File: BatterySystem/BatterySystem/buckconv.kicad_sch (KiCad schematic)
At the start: 0 parts

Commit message: DCDC Converter symbol & footprint
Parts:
- added U1: 3.3V, VR20S3V3:VR20S3V3, symbol custom:VR20S3V3
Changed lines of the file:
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@@
 (kicad_sch (version 20230121) (generator eeschema)
   (paper "A4")
+  (symbol (lib_id "custom:VR20S3V3") (at 135.89 80.01 0) (unit 1)
+    (in_bom yes) (on_board yes) (dnp no) (fields_autoplaced)
+    (property "Reference" "U1" (at 141.605 80.3268 0)
+      (effects (font (size 1.27 1.27)) (justify left))
+    )
+    (property "Value" "3.3V" (at 135.89 80.01 0)
+      (effects (font (size 1.27 1.27)) hide)
+    )
+    (property "Footprint" "VR20S3V3:VR20S3V3" (at 135.89 80.01 0)
+      (effects (font (size 1.27 1.27)) hide)
+    )
+    (property "Datasheet" "https://www.farnell.com/datasheets/3103815.pdf" (at 135.89 80.01 0)
+      (effects (font (size 1.27 1.27)) hide)
+    )
+    (pin "2")
+    (pin "3")
+    (pin "1")
+    (instances
+      (project "BatterySystem"
+        (path "/087df5f5-f8bd-4aad-837d-9ee553cf1b81/a03965c6-cfc0-427e-8817-8deee22f0563"
+          (reference "U1") (unit 1)
+        )
+      )
+    )
+  )
 )

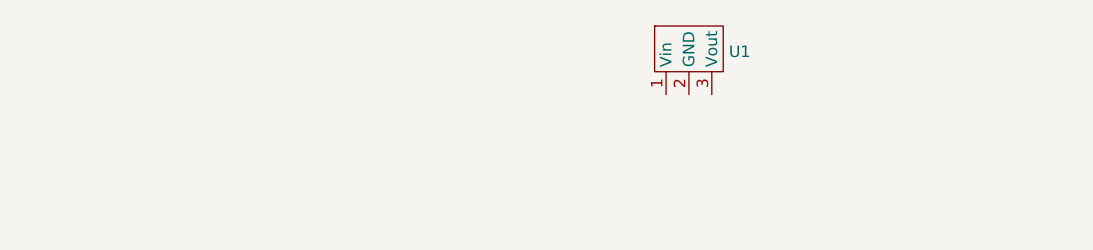
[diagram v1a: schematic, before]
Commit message: Circuit  of the DCDC conv
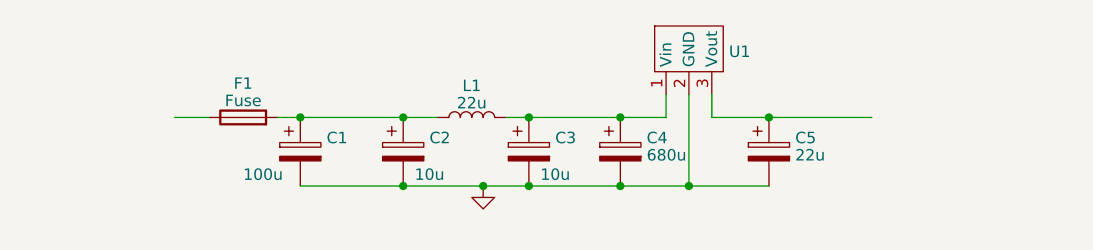
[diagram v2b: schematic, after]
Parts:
- added C1: 100u, symbol Device:C_Polarized
- added C2, C3: 10u, symbol Device:C_Polarized
- added C4: 680u, symbol Device:C_Polarized
- added C5: 22u, symbol Device:C_Polarized
- added F1: Fuse, symbol Device:Fuse
- added L1: 22u, symbol Device:L
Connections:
- net at U1.1 (Vin): now also C3.1, C4.1, L1.2
- net GND: now reaches U1.2 (GND)
- net GND: now also C1.2, C2.2, C3.2, C4.2, C5.2
- net at U1.3 (Vout): now also C5.1
- new net: C1.1, C2.1, F1.2, L1.1

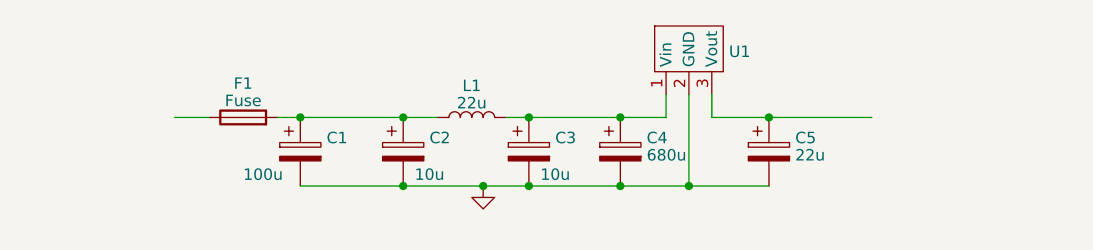
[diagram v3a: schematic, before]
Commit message: USB toegevoegd
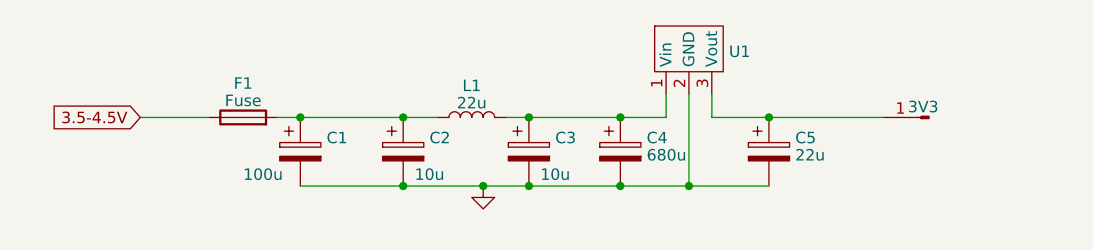
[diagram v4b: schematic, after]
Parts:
- added 3V3: Conn_01x01_Pin, symbol Connector:Conn_01x01_Pin
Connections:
- net at C5.1, U1.3 (Vout): now also 3V3.1 (Pin_1)
- net 3.5-4.5V: now reaches F1.1
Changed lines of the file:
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@@
-    (stroke (width 0) (type default))
-  )
-  (wire (pts (xy 146.05 87.63) (xy 157.48 87.63))
     (stroke (width 0) (type default))
   )
@@
     (stroke (width 0) (type default))
   )
-  (wire (pts (xy 80.01 87.63) (xy 83.82 87.63))
+  (wire (pts (xy 146.05 87.63) (xy 158.75 87.63))
     (stroke (width 0) (type default))
   )
   (wire (pts (xy 137.16 85.09) (xy 137.16 95.25))
+    (stroke (width 0) (type default))
+  )
+  (wire (pts (xy 76.2 87.63) (xy 83.82 87.63))
     (stroke (width 0) (type default))
   )
@@
   (wire (pts (xy 93.98 87.63) (xy 105.41 87.63))
     (stroke (width 0) (type default))
+  )
+  (global_label "3.5-4.5V" (shape input) (at 76.2 87.63 180) (fields_autoplaced)
+    (effects (font (size 1.27 1.27)) (justify right))
+    (property "Intersheetrefs" "${INTERSHEET_REFS}" (at 64.5856 87.63 0)
+      (effects (font (size 1.27 1.27)) (justify right) hide)
+    )
   )
   (symbol (lib_id "Device:C_Polarized") (at 93.98 91.44 0) (unit 1)
@@
         )
       )
+    )
+  )
+  (symbol (lib_id "Connector:Conn_01x01_Pin") (at 163.83 87.63 180) (unit 1)
+    (in_bom yes) (on_board yes) (dnp no) (fields_autoplaced)
+    (property "Reference" "3V3" (at 163.195 86.4649 0)
+      (effects (font (size 1.27 1.27)))
+    )
+    (property "Value" "Conn_01x01_Pin" (at 163.195 88.7951 0)
+      (effects (font (size 1.27 1.27)) hide)
+    )
+    (property "Footprint" "" (at 163.83 87.63 0)
+      (effects (font (size 1.27 1.27)) hide)
+    )
+    (property "Datasheet" "~" (at 163.83 87.63 0)
+      (effects (font (size 1.27 1.27)) hide)
+    )
+    (pin "1")
+    (instances
+      (project "BatterySystem"
+        (path "/087df5f5-f8bd-4aad-837d-9ee553cf1b81/a03965c6-cfc0-427e-8817-8deee22f0563"
+          (reference "3V3") (unit 1)
+        )
+      )

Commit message: footprint buckconv
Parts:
- C1: footprint (none) -> Capacitor_THT:CP_Radial_D8.0mm_P3.50mm
- C2, C3: footprint (none) -> Capacitor_SMD:C_1206_3216Metric
- C4: footprint (none) -> Capacitor_THT:CP_Radial_D12.5mm_P5.00mm
- C5: footprint (none) -> Capacitor_SMD:C_0805_2012Metric
- L1: footprint (none) -> Inductor_SMD:L_Bourns_SRP1038C_10.0x10.0mm
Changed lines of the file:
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@@
       (effects (font (size 1.27 1.27)) (justify left))
     )
-    (property "Footprint" "" (at 94.9452 95.25 0)
+    (property "Footprint" "Capacitor_THT:CP_Radial_D8.0mm_P3.50mm" (at 94.9452 95.25 0)
       (effects (font (size 1.27 1.27)) hide)
     )
@@
       (effects (font (size 1.27 1.27)) (justify left))
     )
-    (property "Footprint" "" (at 120.3452 95.25 0)
+    (property "Footprint" "Capacitor_SMD:C_1206_3216Metric" (at 120.3452 95.25 0)
       (effects (font (size 1.27 1.27)) hide)
     )
@@
       (effects (font (size 1.27 1.27)) (justify left))
     )
-    (property "Footprint" "" (at 147.0152 95.25 0)
+    (property "Footprint" "Capacitor_SMD:C_0805_2012Metric" (at 147.0152 95.25 0)
       (effects (font (size 1.27 1.27)) hide)
     )
@@
       (effects (font (size 1.27 1.27)) (justify left))
     )
-    (property "Footprint" "" (at 106.3752 95.25 0)
+    (property "Footprint" "Capacitor_SMD:C_1206_3216Metric" (at 106.3752 95.25 0)
       (effects (font (size 1.27 1.27)) hide)
     )
@@
       (effects (font (size 1.27 1.27)))
     )
-    (property "Footprint" "" (at 113.03 87.63 0)
+    (property "Footprint" "Inductor_SMD:L_Bourns_SRP1038C_10.0x10.0mm" (at 113.03 87.63 0)
       (effects (font (size 1.27 1.27)) hide)
     )
@@
       (effects (font (size 1.27 1.27)) (justify left))
     )
-    (property "Footprint" "" (at 130.5052 95.25 0)
+    (property "Footprint" "Capacitor_THT:CP_Radial_D12.5mm_P5.00mm" (at 130.5052 95.25 0)
       (effects (font (size 1.27 1.27)) hide)
     )

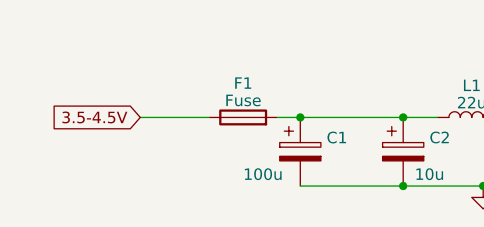
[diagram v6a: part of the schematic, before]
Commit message: Batterij en houder toegevoegd
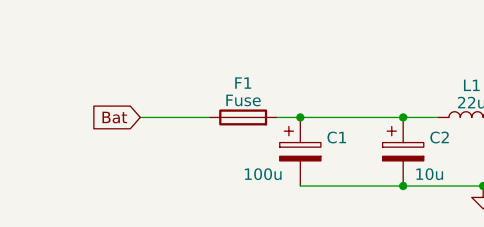
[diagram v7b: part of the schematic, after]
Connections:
- net 3.5-4.5V renamed Bat
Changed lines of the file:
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@@
     (stroke (width 0) (type default))
   )
-  (global_label "3.5-4.5V" (shape input) (at 76.2 87.63 180) (fields_autoplaced)
+  (global_label "Bat" (shape input) (at 76.2 87.63 180) (fields_autoplaced)
     (effects (font (size 1.27 1.27)) (justify right))
-    (property "Intersheetrefs" "${INTERSHEET_REFS}" (at 64.5856 87.63 0)
+    (property "Intersheetrefs" "${INTERSHEET_REFS}" (at 70.1495 87.63 0)
       (effects (font (size 1.27 1.27)) (justify right) hide)
     )

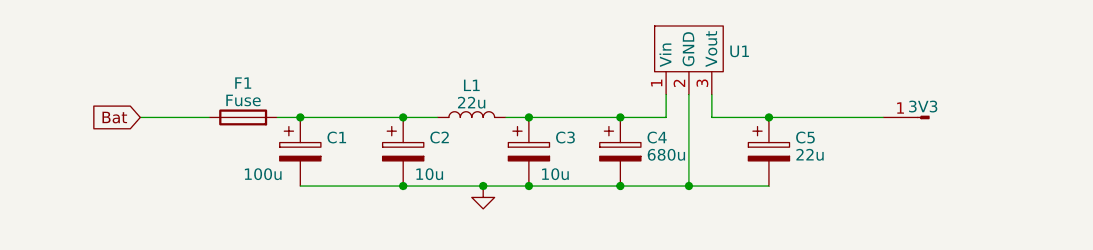
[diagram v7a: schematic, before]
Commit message: Componenten footprint toegevoegd
usb c footprint is met niks aangesloten. raar
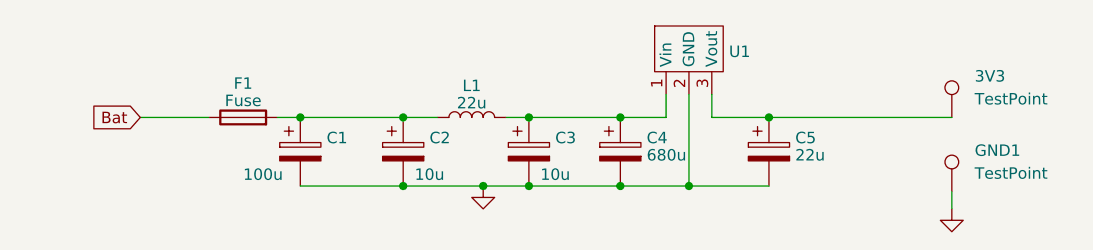
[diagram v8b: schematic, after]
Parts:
- removed 3V3: Conn_01x01_Pin, symbol Connector:Conn_01x01_Pin
- added 3V3, GND1: TestPoint, TestPoint:TestPoint_Keystone_5005-5009_Compact, symbol Connector:TestPoint
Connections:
- net GND: now also GND1.1
- net at C5.1, U1.3 (Vout): now also 3V3.1
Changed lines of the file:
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@@
+    (stroke (width 0) (type default))
+  )
+  (wire (pts (xy 166.37 95.885) (xy 166.37 97.79))
     (stroke (width 0) (type default))
   )
@@
     (stroke (width 0) (type default))
   )
-  (wire (pts (xy 146.05 87.63) (xy 158.75 87.63))
+  (wire (pts (xy 146.05 87.63) (xy 166.37 87.63))
     (stroke (width 0) (type default))
   )
@@
     )
   )
-  (symbol (lib_id "Connector:Conn_01x01_Pin") (at 163.83 87.63 180) (unit 1)
-    (in_bom yes) (on_board yes) (dnp no) (fields_autoplaced)
-    (property "Reference" "3V3" (at 163.195 86.4649 0)
-      (effects (font (size 1.27 1.27)))
-    )
-    (property "Value" "Conn_01x01_Pin" (at 163.195 88.7951 0)
-      (effects (font (size 1.27 1.27)) hide)
-    )
-    (property "Footprint" "" (at 163.83 87.63 0)
-      (effects (font (size 1.27 1.27)) hide)
-    )
-    (property "Datasheet" "~" (at 163.83 87.63 0)
-      (effects (font (size 1.27 1.27)) hide)
-    )
-    (pin "1")
-    (instances
-      (project "BatterySystem"
-        (path "/087df5f5-f8bd-4aad-837d-9ee553cf1b81/a03965c6-cfc0-427e-8817-8deee22f0563"
-          (reference "3V3") (unit 1)
-        )
-      )
-    )
-  )
   (symbol (lib_id "Device:C_Polarized") (at 105.41 91.44 0) (unit 1)
     (in_bom yes) (on_board yes) (dnp no)
@@
     )
   )
+  (symbol (lib_id "Connector:TestPoint") (at 166.37 95.885 0) (unit 1)
+    (in_bom yes) (on_board yes) (dnp no) (fields_autoplaced)
+    (property "Reference" "GND1" (at 168.91 91.313 0)
+      (effects (font (size 1.27 1.27)) (justify left))
+    )
+    (property "Value" "TestPoint" (at 168.91 93.853 0)
+      (effects (font (size 1.27 1.27)) (justify left))
+    )
+    (property "Footprint" "TestPoint:TestPoint_Keystone_5005-5009_Compact" (at 171.45 95.885 0)
+      (effects (font (size 1.27 1.27)) hide)
+    )
+    (property "Datasheet" "~" (at 171.45 95.885 0)
+      (effects (font (size 1.27 1.27)) hide)
+    )
+    (pin "1")
+    (instances
+      (project "BatterySystem"
+        (path "/087df5f5-f8bd-4aad-837d-9ee553cf1b81/a03965c6-cfc0-427e-8817-8deee22f0563"
+          (reference "GND1") (unit 1)
+        )
+      )
+    )
+  )
+  (symbol (lib_id "power:GND") (at 166.37 97.79 0) (unit 1)
+    (in_bom yes) (on_board yes) (dnp no) (fields_autoplaced)
+    (property "Reference" "#PWR013" (at 166.37 104.14 0)
+      (effects (font (size 1.27 1.27)) hide)
+    )
+    (property "Value" "GND" (at 166.37 101.9255 0)
+      (effects (font (size 1.27 1.27)) hide)
+    )
+    (property "Footprint" "" (at 166.37 97.79 0)
+      (effects (font (size 1.27 1.27)) hide)
+    )
+    (property "Datasheet" "" (at 166.37 97.79 0)
+      (effects (font (size 1.27 1.27)) hide)
+    )
+    (pin "1")
+    (instances
+      (project "BatterySystem"
+        (path "/087df5f5-f8bd-4aad-837d-9ee553cf1b81/a03965c6-cfc0-427e-8817-8deee22f0563"
+          (reference "#PWR013") (unit 1)
+        )
+      )
+    )
+  )
   (symbol (lib_id "Device:L") (at 113.03 87.63 90) (unit 1)
     (in_bom yes) (on_board yes) (dnp no) (fields_autoplaced)
@@
         )
       )
+    )
+  )
+  (symbol (lib_id "Connector:TestPoint") (at 166.37 87.63 0) (unit 1)
+    (in_bom yes) (on_board yes) (dnp no) (fields_autoplaced)
+    (property "Reference" "3V3" (at 168.91 83.058 0)
+      (effects (font (size 1.27 1.27)) (justify left))
+    )
+    (property "Value" "TestPoint" (at 168.91 85.598 0)
+      (effects (font (size 1.27 1.27)) (justify left))
+    )
+    (property "Footprint" "TestPoint:TestPoint_Keystone_5005-5009_Compact" (at 171.45 87.63 0)
+      (effects (font (size 1.27 1.27)) hide)
+    )
+    (property "Datasheet" "~" (at 171.45 87.63 0)
+      (effects (font (size 1.27 1.27)) hide)
+    )
+    (pin "1")
+    (instances
+      (project "BatterySystem"
+        (path "/087df5f5-f8bd-4aad-837d-9ee553cf1b81/a03965c6-cfc0-427e-8817-8deee22f0563"
+          (reference "3V3") (unit 1)
+        )
+      )
